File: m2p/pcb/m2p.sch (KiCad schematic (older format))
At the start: 59 parts, among them IC1 APU1205-HF-3, IC2 ADuM1201, IC3 SN74AHC1G32DCKR, IC4 SP100-2T, IC5 ADXL375, IC6 ATMEGA328P, P1 CONN_2, P2 CONN_4, P3 CONN_2, P4 CONN_2, P5 CONN_4, Q1 MOSFET_P, Q2 MOSFET_P, Q3 MOSFET_N, Q4 MOSFET_N, U1 BAT BOX, U2 ARM SW, U3 RGB LED, U4 ICSP, X1 8M

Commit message: add battery voltage monitoring
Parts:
- removed P5: CONN_4, symbol CONN_4
- removed R20, R21: 100, 0603, symbol R
- added C10: 2µ2, 0603, symbol CP1
- added C15: 100n, 0603, symbol C
- added P5: CONN_2, symbol CONN_2
- added R3: 10k, 0603, symbol R
- added R4: 1k, 0603, symbol R
- R21: renamed from R19; value 100 -> 50; Farnell 2331989 -> 2331983
- U3: value RGB LED -> RG LED; Farnell 2290375 -> 1142488
- renumbered C10 to C11, C11 to C12, C12 to C13, C13 to C14, C14 to C16, C15 to C17, C16 to C18, R8 to R10, R9 to R11, R10 to R12, R11 to R13, R12 to R14, R13 to R15, R14 to R16, R15 to R17, R16 to R18, R17 to R19, R18 to R20, R3 to R5, R4 to R6, R5 to R7, R6 to R8, R7 to R9
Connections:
- net labels added: LED_A, LED_C
- net labels removed: LED_B, LED_G, LED_R
- wire segments 204 -> 212
- no-connect marks 13 -> 12

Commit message: swap to an STM32 chip
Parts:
- removed C15, C16, C17, C18: 100n, 0603, symbol C
- removed IC3: SN74AHC1G32DCKR, symbol SN74AHC1G32DCKR
- removed IC6: ATMEGA328P, TQFP32, symbol ATMEGA328P
- removed U4: ICSP, symbol ICSP
- added C? (x7): 100n, 0603, symbol C
- added C?: 10µ, 1411, symbol CP1
- added C?: 1µ, 0805, symbol CP1
- added D? (x2): GREEN, 0603, symbol LED
- added D?: RED, 0603, symbol LED
- added D? (x3): YELLOW, 0603, symbol LED
- added IC?: STM32F103C, TQFP48, symbol STM32F103C
- added P?: SWD, symbol SWD
- added R? (x7): 100, 0603, symbol R
- X1: Farnell 1666997 -> 2063945
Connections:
- net labels added: ACCEL_CS, ACCEL_MISO, ACCEL_MOSI, ACCEL_SCK, BARO_CS, BARO_MISO, BARO_MOSI, BARO_SCK, BAT_MON, LED1, LED2, LED3, LED_1, LED_P1C, LED_P2C, PYRO_1_C, PYRO_1_F, PYRO_2_C, PYRO_2_F, SER_IN, SER_OUT, SWCLK, SWDIO, SWO, nRST
- net labels removed: ADXL_CS, MISO, MOSI, PYRO_C_1, PYRO_C_2, PYRO_F_1, PYRO_F_2, RESET, SCK, SERIN, SEROUT, SP100_CS
- wire segments 212 -> 257
- no-connect marks 12 -> 15
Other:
- note added: "BATTERY MONITORING"
- note added: "EXTERNAL STATUS LED"
- note added: "INTERNAL STATUS LEDS"
- note added: "MICROCONTROLLER"
- note added: "SERIAL WIRE DEBUG"
- note removed: "AVR"
- note removed: "STATUS LED"
- moved on the sheet: C10, C11, C12, C13, C14, C8, D1, D2, P3, P4, P5, Q1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

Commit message: annotate parts
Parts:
- gave numbers to parts that had none: 24
- renumbered C12 to C11, C13 to C12, C11 to C22, C14 to C23, D1 to D5, D2 to D6, IC4 to IC3, IC5 to IC4, P5 to P3, P3 to P5, P4 to P6, R7 to R10, R8 to R11, R9 to R12, R10 to R13, R11 to R14, R12 to R15, R13 to R16, R14 to R17, R15 to R20, R16 to R21, R17 to R22, R18 to R23, R19 to R25, R20 to R26, R21 to R5, R3 to R6, R4 to R7, R5 to R8, R6 to R9

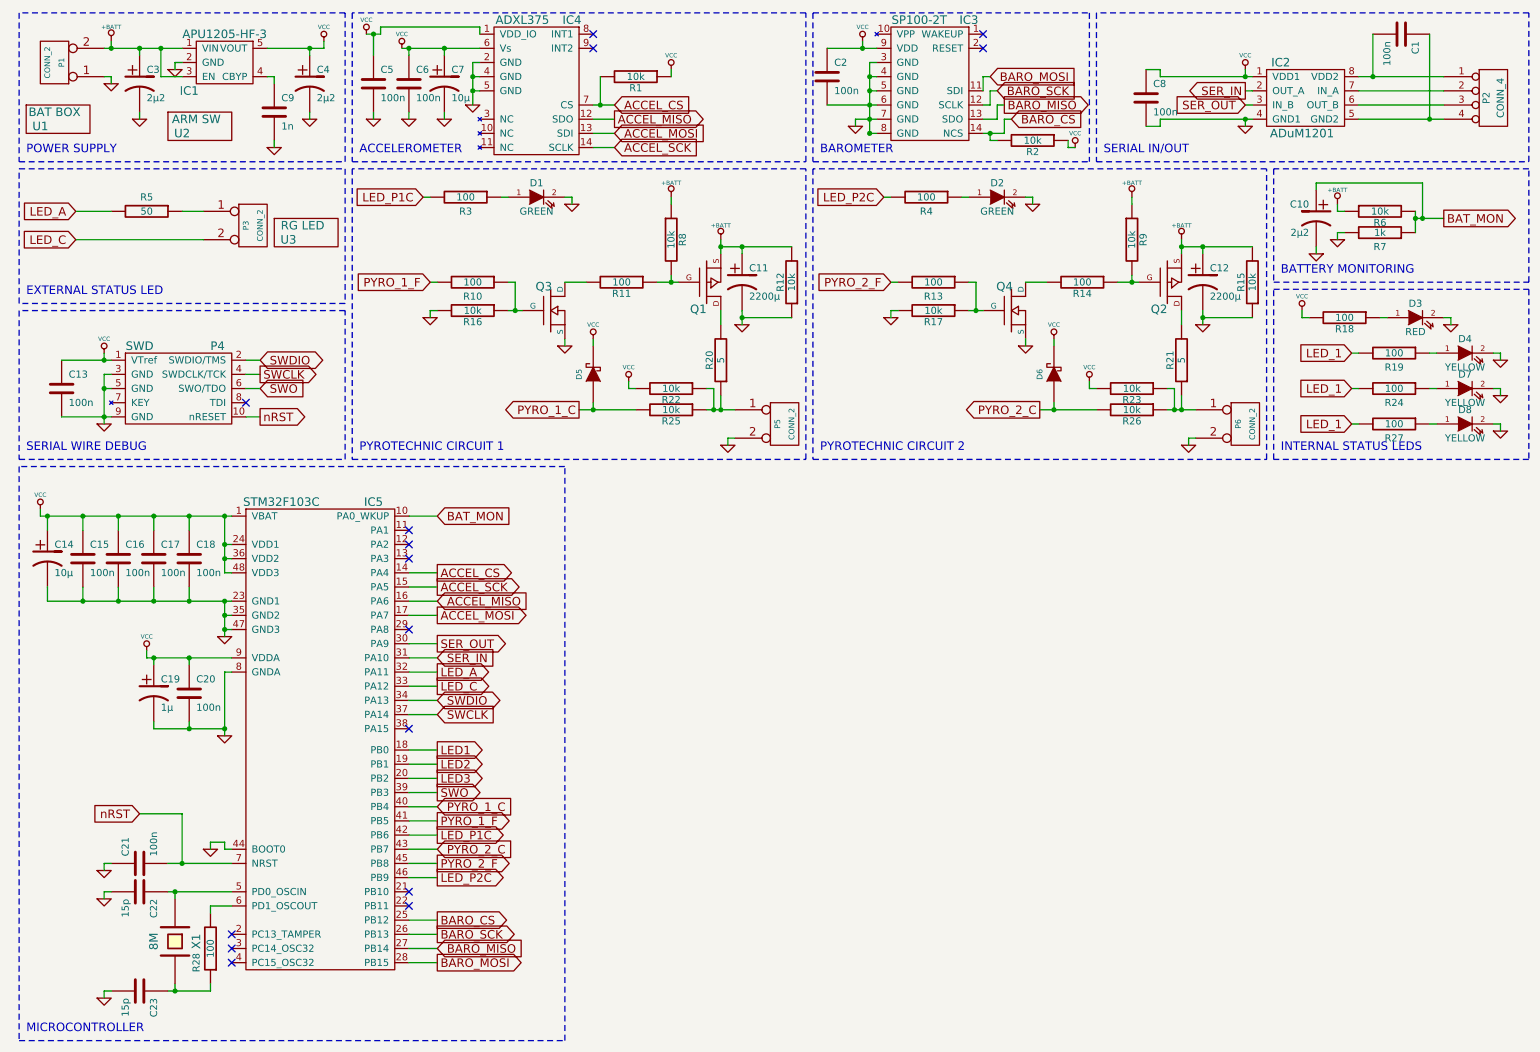
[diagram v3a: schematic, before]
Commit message: fix a few typos
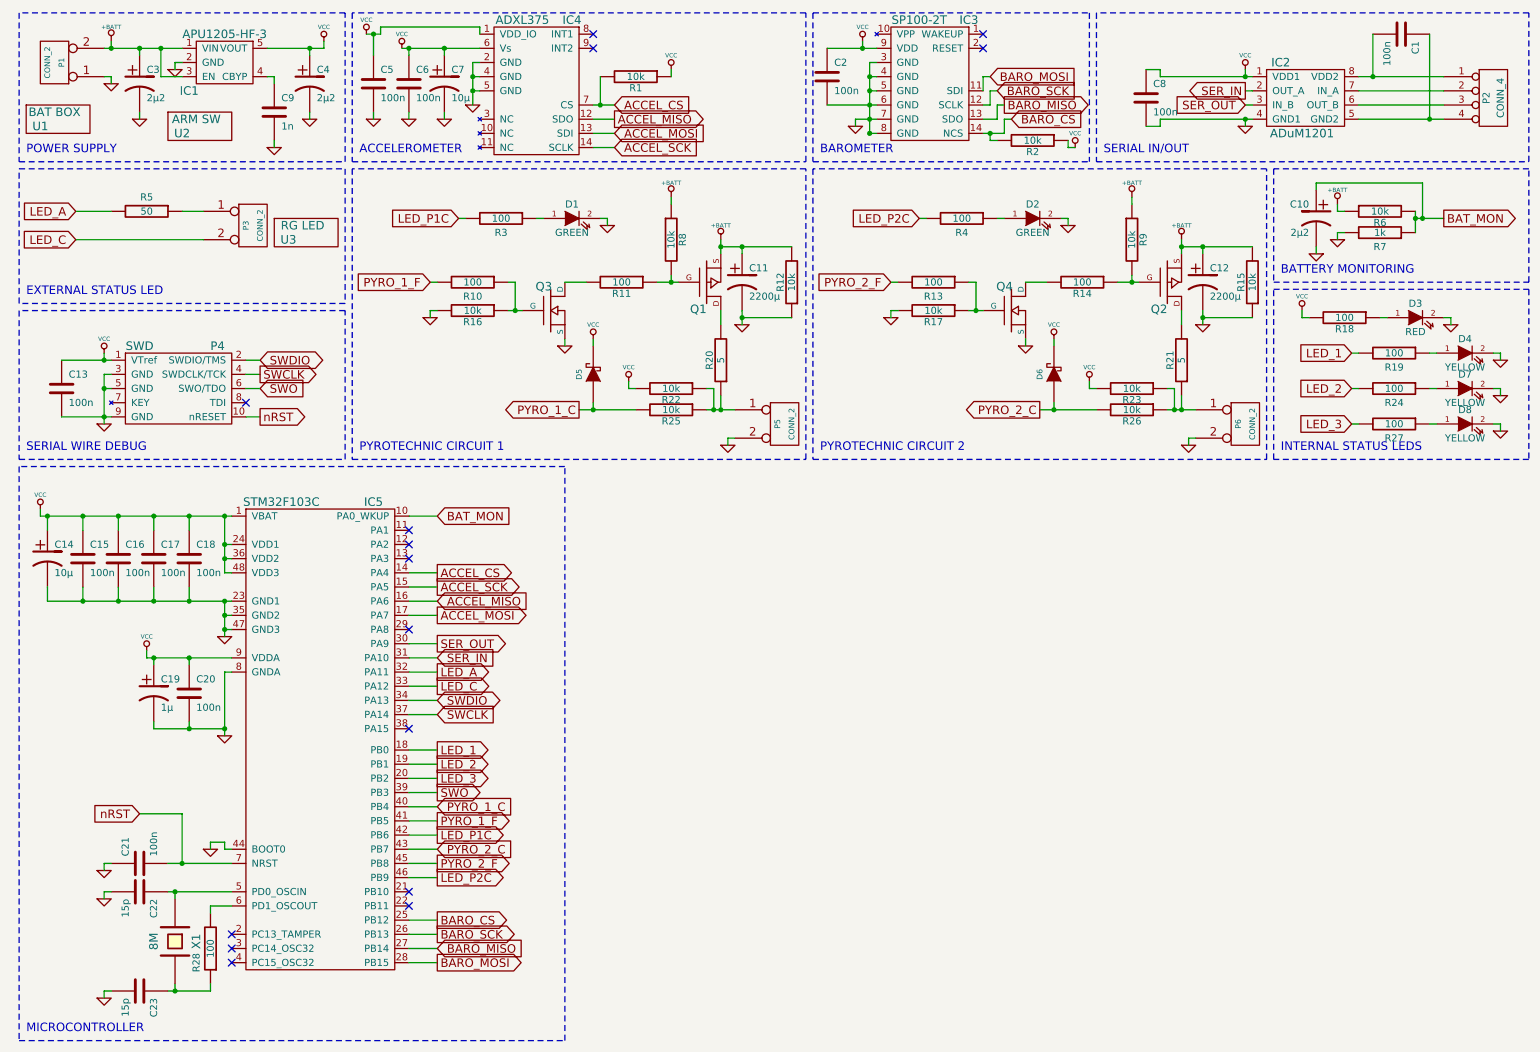
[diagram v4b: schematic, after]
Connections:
- net LED1 is gone; now on net LED_1: IC5.18 (PB0)
- net LED_1: no longer R24.2, R27.2
- net LED2 renamed LED_2
- net LED_2: now also R24.2
- net LED3 renamed LED_3
- net LED_3: now also R27.2
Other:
- moved on the sheet: D1, D2, R3, R4

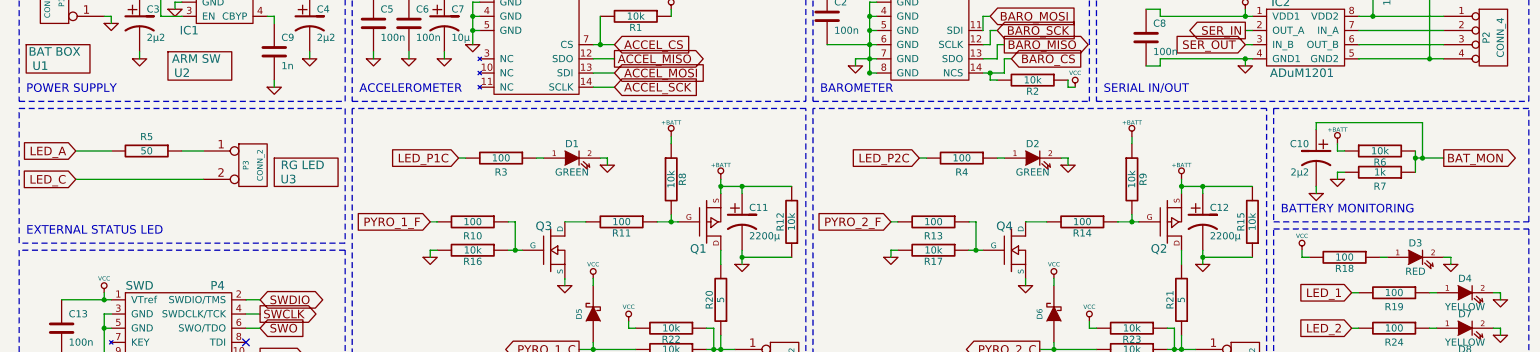
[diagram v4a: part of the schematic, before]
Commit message: rearrange LEDs a little
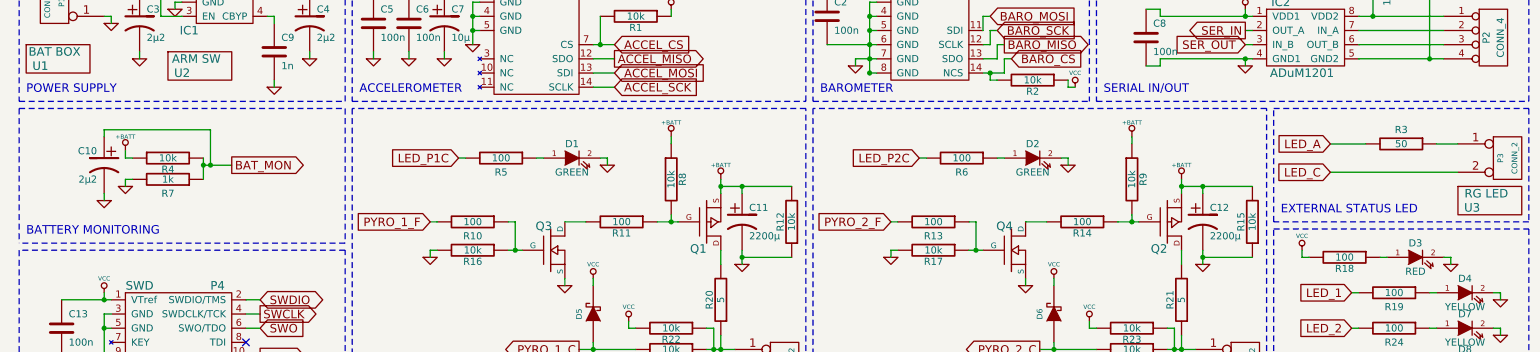
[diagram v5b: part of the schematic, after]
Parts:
- renumbered R5 to R3, R6 to R4, R3 to R5, R4 to R6
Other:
- moved on the sheet: C10, P3, R3, R4, R7, U3

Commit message: respec parts for stock level
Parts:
- C11, C12: Farnell 2346510 -> 2346569
- R20, R21: Farnell 2328359 -> 2328356
- R7: Farnell 2332003 -> 2331727

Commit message: stm32 is lqfp package
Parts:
- IC5: footprint TQFP48 -> LQFP48
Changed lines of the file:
@@
 F 0 "IC5" H 3000 7250 60  0000 C CNN
 F 1 "STM32F103C" H 2350 7250 60  0000 C CNN
-F 2 "TQFP48" H 2750 5800 60  0001 C CNN
+F 2 "LQFP48" H 2750 5800 60  0001 C CNN
 F 3 "" H 2750 5800 60  0000 C CNN
 F 4 "1447637" H 2650 5600 60  0001 C CNN "Farnell"

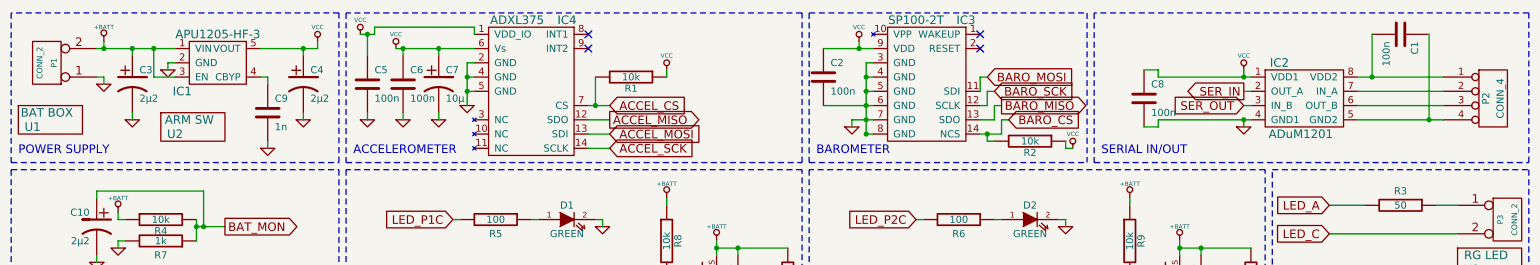
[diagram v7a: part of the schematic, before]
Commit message: add power flags so ERC all pass
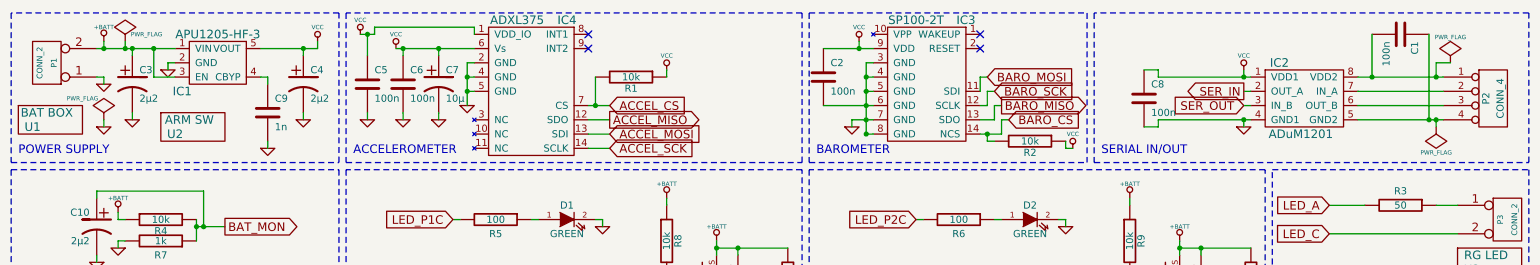
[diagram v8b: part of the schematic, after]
